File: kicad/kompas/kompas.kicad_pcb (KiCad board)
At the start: 2 copper layers, 59.2 x 130 mm, 81 parts, among them J10 Conn_01x10_Male, J11 Conn_01x10_Male, J12 Conn_01x10_Male, J13 Conn_01x10_Male, J14 Conn_01x10_Male, J15 Conn_01x10_Male, J16 Conn_01x10_Male, J18 Conn_01x10_Male, J19 Conn_01x10_Male, J20 Conn_01x10_Male, J4 Conn_02x05_Odd_Even, J5 Conn_01x06, J6 Conn_01x10_Male, J7 Conn_01x10_Male, J8 Conn_01x10_Male, J9 Conn_01x10_Male, Q1 2N3904, Q2 2N3904, Q3 2N3904, Q4 2N3904, Q5 2N3904, U1 ATmega328-AU, U2 MCP6004, U3 7805_PINS, Y1 Crystal_GND2

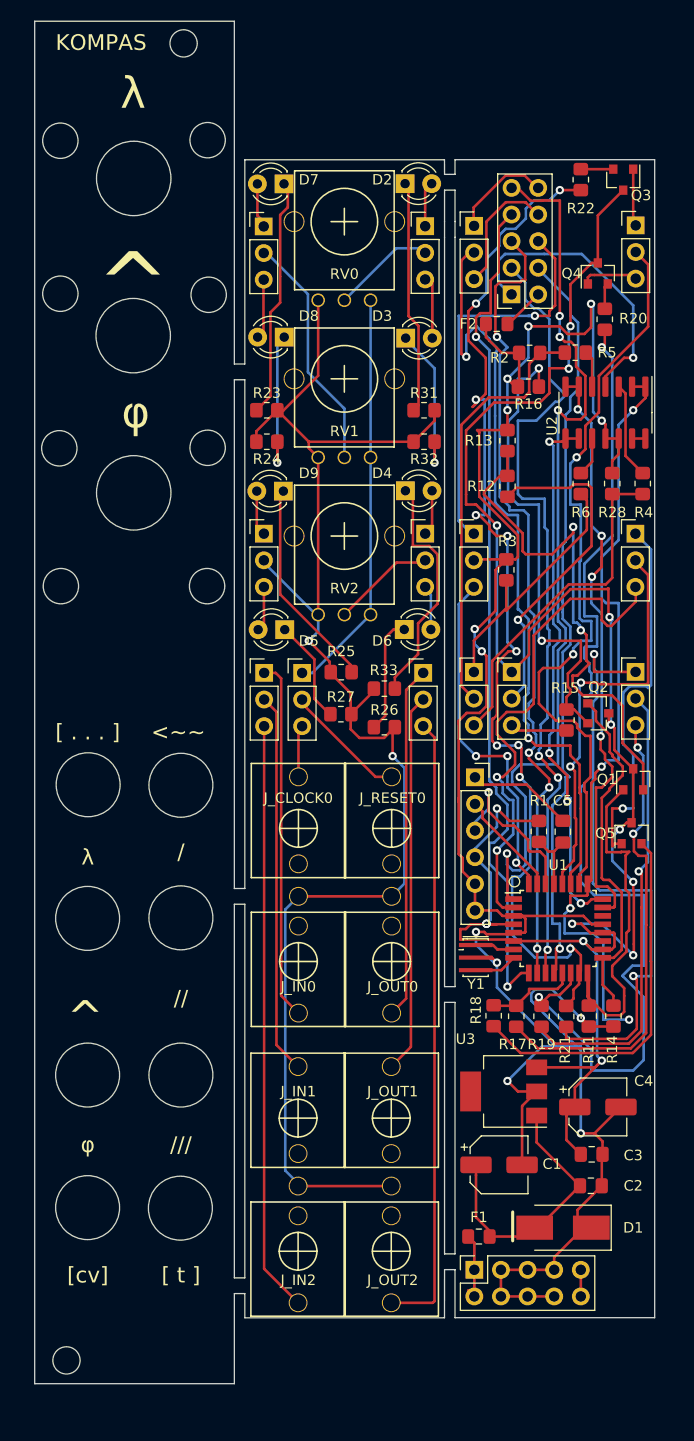
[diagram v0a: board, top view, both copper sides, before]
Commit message: fix transistors
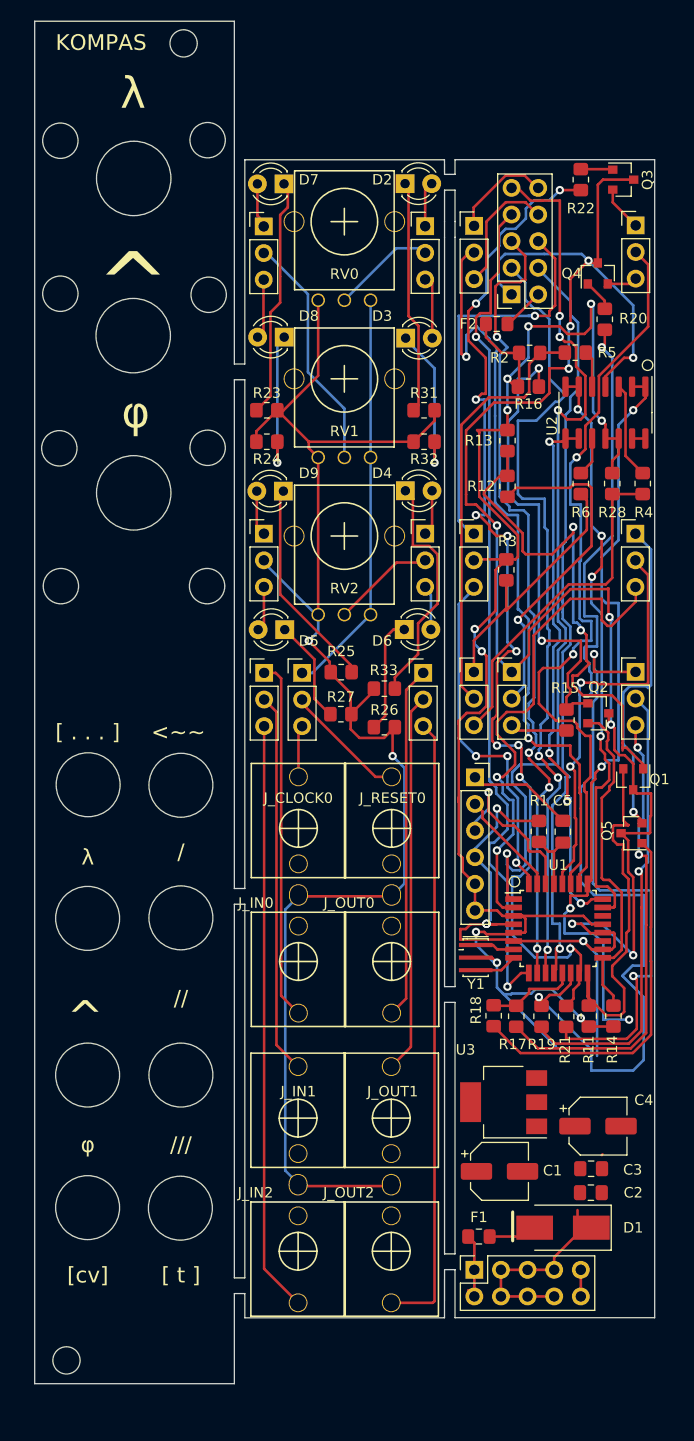
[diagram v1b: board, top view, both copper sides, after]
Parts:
- removed G***: LOGO, custom_eurorack:mates_smaller
- J_IN0, J_IN2, J_OUT0, J_OUT2: value PJ301M-12_without_ground -> PJ301M-12; footprint custom_eurorack:PJ301M-12_without_ground -> eurocad:PJ301M-12
- moved C4 1.83 mm to (122.6, 130.3)
- moved C3 1.37 mm to (121.9, 134.4)
- moved U3 1.02 mm to (113.6, 128.0)
- moved C2 0.66 mm to (121.9, 136.7)
- moved C1 0.63 mm to (113.2, 134.6)
- turned Q1 to 270 degrees
- turned Q3 to 0 degrees
- turned Q5 to 180 degrees
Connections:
- Q1 pad 1: RESET -> Net-(Q1-Pad1)
- Q1 pad 2: Net-(Q1-Pad2) -> RESET
- Q2 pad 1: CLOCK -> Net-(Q2-Pad1)
- Q2 pad 2: Net-(Q2-Pad2) -> CLOCK
- Q3 pad 1: OUT_LED0_B -> Net-(Q3-Pad1)
- Q3 pad 2: Net-(Q3-Pad2) -> OUT_LED0_B
- Q4 pad 1: OUT_LED1_B -> Net-(Q4-Pad1)
- Q4 pad 2: Net-(Q4-Pad2) -> OUT_LED1_B
- Q5 pad 1: OUT_LED2_B -> Net-(Q5-Pad1)
- Q5 pad 2: Net-(Q5-Pad2) -> OUT_LED2_B
- R12 pad 1: Net-(Q1-Pad2) -> Net-(Q1-Pad1)
- R13 pad 1: Net-(Q1-Pad2) -> Net-(Q1-Pad1)
- R15 pad 1: Net-(Q2-Pad2) -> Net-(Q2-Pad1)
- R16 pad 1: Net-(Q2-Pad2) -> Net-(Q2-Pad1)
- R18 pad 1: Net-(Q5-Pad2) -> Net-(Q5-Pad1)
- R20 pad 1: Net-(Q4-Pad2) -> Net-(Q4-Pad1)
- R22 pad 1: Net-(Q3-Pad2) -> Net-(Q3-Pad1)
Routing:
- net Net-(Q1-Pad2): track 50.0 -> 0.00 mm, vias 2 -> 0
- net Net-(Q1-Pad1): track 0.00 -> 48.5 mm, vias 0 -> 2
- net Net-(Q2-Pad2): track 47.0 -> 0.00 mm, vias 2 -> 0
- net Net-(Q2-Pad1): track 0.00 -> 46.7 mm, vias 0 -> 2
- net GND_B: track 222.3 -> 176.1 mm, vias 12 -> 10
- net Net-(Q5-Pad1): track 0.00 -> 35.4 mm
- net Net-(Q5-Pad2): track 35.4 -> 0.00 mm
- net Net-(C1-Pad1): track 26.4 -> 4.68 mm
- net VCC_B: track 222.5 -> 211.2 mm, vias 15 -> 13
- net OUT_LED2_B: track 36.9 -> 32.0 mm
- net Net-(Q3-Pad2): track 3.10 -> 0.00 mm
- net Net-(Q3-Pad1): track 0.00 -> 3.07 mm
- net Net-(Q4-Pad1): track 0.00 -> 3.04 mm
- net Net-(Q4-Pad2): track 2.49 -> 0.00 mm
- net OUT_LED1_B: track 5.30 -> 3.28 mm
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
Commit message: adapt headers
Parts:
- J5: value Conn_01x06 -> Conn_01x07; footprint Connector_PinSocket_2.54mm:PinSocket_1x06_P2.54mm_Vertical -> Connector_PinSocket_2.54mm:PinSocket_1x07_P2.54mm_Vertical
- moved R21 41.2 mm to (100.1, 83.6), turned to 0 degrees
- moved R19 32.6 mm to (98.1, 93.5), turned to 0 degrees
- moved R17 28.3 mm to (102.1, 94.5), turned to 180 degrees
- moved R18 16.6 mm to (127.0, 111.5), turned to 270 degrees
- moved R14 5.20 mm to (118.9, 119.6)
- moved Y1 3.90 mm to (111.3, 118.1), turned to 0 degrees
- moved R33 1.69 mm to (102.2, 86.9)
- moved R26 0.80 mm to (102.2, 91.4)
- moved R11 0.54 mm to (121.4, 119.4)
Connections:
- J10 pad 1: OUT0_B -> OUT0
- J10 pad 2: OUT1_B -> OUT1
- J10 pad 3: OUT2_B -> OUT2
- J4 pad 3: PD7 -> SCK
- J4 pad 4: PB0 -> MISO
- J5 pad 6: GND_B -> SDA
- J_OUT0 pad 3: OUT0_T -> Net-(J_OUT0-Pad3)
- J_OUT1 pad 3: OUT1_T -> Net-(J_OUT1-Pad3)
- J_OUT2 pad 3: OUT2_T -> Net-(J_OUT2-Pad3)
- R17 pad 1: OUT2_B -> Net-(J_OUT2-Pad3)
- R17 pad 2: OUT2 -> OUT2_T
- R19 pad 1: OUT1_B -> Net-(J_OUT1-Pad3)
- R19 pad 2: OUT1 -> OUT1_T
- R21 pad 1: OUT0_B -> Net-(J_OUT0-Pad3)
- R21 pad 2: OUT0 -> OUT0_T
- U1 pad 1: LED0 -> OUT0
- U1 pad 11: PD7 -> CLOCK
- U1 pad 12: PB0 -> RESET
- U1 pad 15: OUT0 -> LED0
- U1 pad 16: RESET -> MISO
- U1 pad 17: CLOCK -> SCK
- U1 pad 19: Net-(U1-Pad19) -> POT1_B
- U1 pad 22: Net-(U1-Pad22) -> POT2_B
- U1 pad 27: POT1_B -> SDA
- U1 pad 28: POT2_B -> SCL
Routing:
- net SCK: track 0.00 -> 96.1 mm, vias 0 -> 4
- net PD7: track 77.3 -> 0.00 mm, vias 3 -> 0
- net MISO: track 0.00 -> 74.6 mm, vias 0 -> 1
- net PB0: track 73.4 -> 0.00 mm, vias 1 -> 0
- net Net-(J_OUT2-Pad3): track 0.00 -> 59.7 mm
- net OUT0_B: track 56.9 -> 0.00 mm, vias 2 -> 0
- net OUT2_T: track 59.5 -> 5.80 mm
- net Net-(J_OUT0-Pad3): track 0.00 -> 45.7 mm, vias 0 -> 1
- net OUT2_B: track 45.0 -> 0.00 mm, vias 2 -> 0
- net OUT1_B: track 43.6 -> 0.00 mm, vias 1 -> 0
- net Net-(J_OUT1-Pad3): track 0.00 -> 37.1 mm
- net OUT1: track 94.0 -> 129.2 mm, vias 2 -> 6
- net OUT2: track 8.71 -> 42.0 mm, vias 0 -> 2
- net GND_B: track 176.1 -> 206.9 mm, vias 10 -> 8
- net OUT1_T: track 36.3 -> 8.46 mm, vias 0 -> 1
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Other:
- outline, holes or cut-outs redrawn

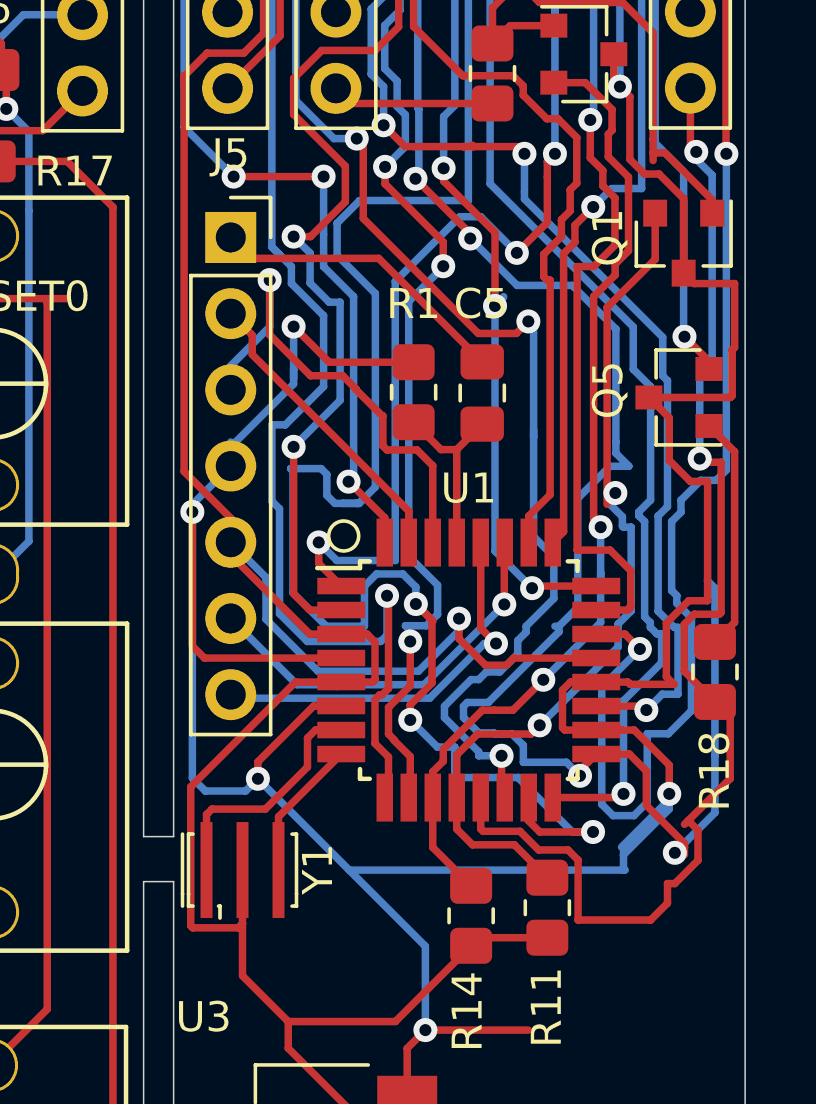
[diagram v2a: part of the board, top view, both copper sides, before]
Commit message: add SS header
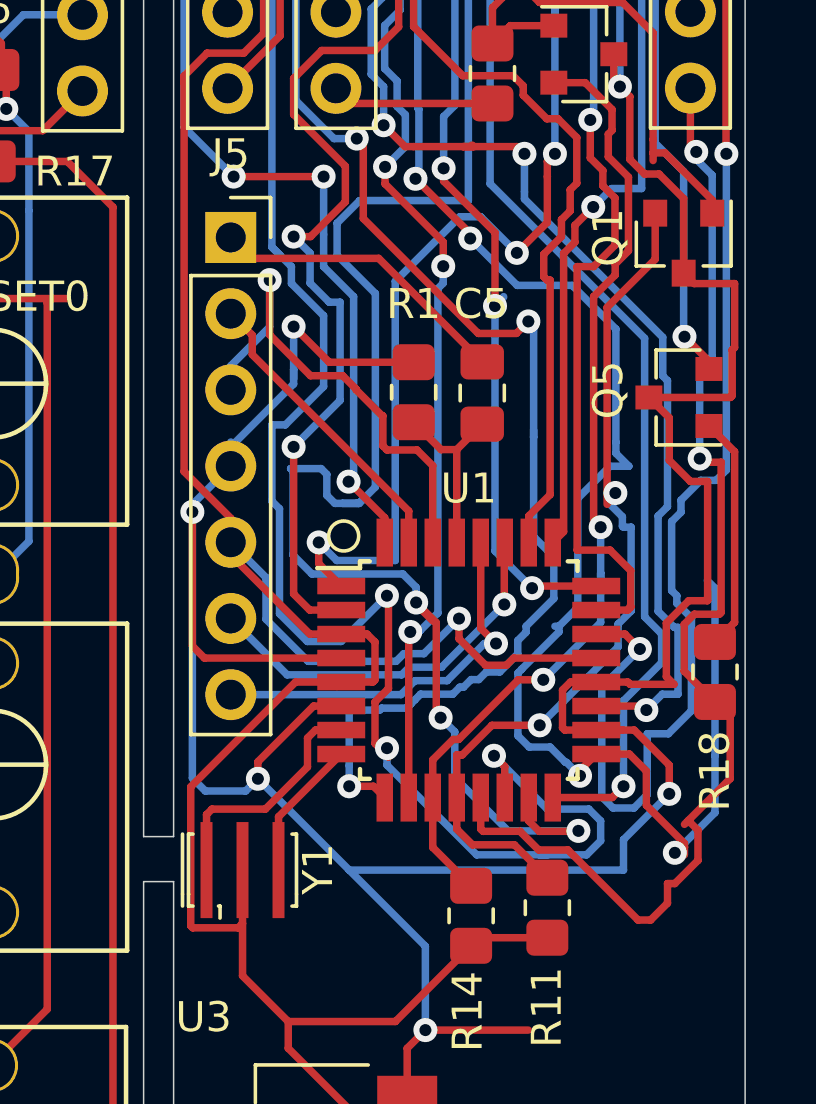
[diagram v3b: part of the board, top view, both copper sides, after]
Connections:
- U1 pad 14: OUT1 -> LED1
- U1 pad 9: LED1 -> OUT1
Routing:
- net LED1: track 84.5 -> 98.9 mm, vias 2 -> 4
- net LED0: track 111.8 -> 107.2 mm
- net OUT1: track 129.2 -> 132.2 mm
- net SCK: track 96.1 -> 93.2 mm
- net VCC_B: track 236.4 -> 233.8 mm
- net LED2: track 78.5 -> 77.1 mm
- net OUT2: track 42.0 -> 40.8 mm
- net MISO: track 74.6 -> 74.0 mm
- net POT2_B: track 51.4 -> 50.9 mm
- net GND_B: track 206.9 -> 206.4 mm
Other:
- board text added: "MISO|PB4"
- board text added: "MOSI|LED0"
- board text added: "SCK|PB5"
- board text added: "SCL"
- board text added: "SDA"
- board text added: "SS|LED1"
- board text removed: "LED0"
- board text removed: "LED1"
- board text removed: "PB0"
- board text removed: "PD7"

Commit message: fixup reset pin
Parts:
- removed C5: 100n, Capacitor_SMD:C_0805_2012Metric_Pad1.18x1.45mm_HandSolder
- J_IN0, J_IN2, J_OUT0, J_OUT2: value PJ301M-12 -> PJ301M-12-2hole; footprint eurocad:PJ301M-12 -> graphics:PJ301M-12-2hole
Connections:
- J5 pad 1: Net-(C5-Pad1) -> RST
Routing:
- net RST: track 6.11 -> 17.8 mm
- net Net-(C5-Pad1): track 10.1 -> 0.00 mm
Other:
- board text added: "KOMPAS STZIOPA // BASTL ___________________ | smd by PHILOMATES | | bottom__rev 2 |"
- board text added: "|smd by PHILOMATES| top__rev2"
- board text removed: "JLCJLCJLCJLC"
- board text removed: "KOMPAS STZIOPA // BASTL ___________________ | smd by PHILOMATES | | bottom__rev 1 |"
- board text removed: "|smd by PHILOMATES| top__rev1"

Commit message: rev3
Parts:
- removed F2: Polyfuse, Fuse:Fuse_0805_2012Metric_Pad1.15x1.40mm_HandSolder
- added G***: LOGO, graphics:mates, B.Cu at (118.6, 121.2)
- J4: footprint Connector_PinSocket_2.54mm:PinSocket_2x05_P2.54mm_Vertical -> Connector_PinSocket_2.54mm:PinSocket_2x04_P2.54mm_Vertical
- R17, R19, R21, R23, R24, R25, R26, R27, R31, R32, R33: moved to B.Cu
- moved R25 23.9 mm to (91.4, 64.0), turned to 270 degrees
- moved R23 22.8 mm to (98.4, 40.4)
- moved R31 16.9 mm to (98.4, 47.0), turned to 180 degrees
- moved R17 14.8 mm to (98.0, 108.7), turned to 90 degrees
- moved R33 14.7 mm to (98.3, 72.6)
- moved R24 12.1 mm to (98.1, 55.1)
- moved R19 10.3 mm to (90.4, 100.3), turned to 90 degrees
- moved R27 9.57 mm to (98.3, 100.6), turned to 90 degrees
- moved R26 9.03 mm to (106.2, 99.6), turned to 270 degrees
- moved R32 8.90 mm to (98.1, 61.0)
- moved R21 3.74 mm to (98.3, 80.3)
- moved RV2 2.88 mm to (98.4, 76.9)
- moved J4 2.48 mm to (114.4, 48.5)
- moved D6 1.19 mm to (105.0, 83.7), turned to 45 degrees
- moved D5 0.98 mm to (92.1, 83.7), turned to 135 degrees
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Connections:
- J4 pad 1: VCC_B -> SCK
- J4 pad 2: Net-(F2-Pad2) -> MISO
- J4 pad 3: SCK -> LED2
- J4 pad 4: MISO -> LED2_A_B
- J4 pad 5: LED2 -> LED1
- J4 pad 6: LED2_A_B -> LED1_A_B
- J4 pad 7: LED1 -> LED0
- J4 pad 8: LED1_A_B -> LED0_A_B
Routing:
- net Net-(D4-Pad1): track 28.2 -> 6.14 mm
- net Net-(J_OUT2-Pad3): track 59.7 -> 39.4 mm
- net Net-(D7-Pad1): track 23.0 -> 4.81 mm
- net Net-(D5-Pad1): track 9.84 -> 24.7 mm, vias 0 -> 2
- net OUT2_T: track 5.80 -> 20.5 mm
- net GND_T: track 143.4 -> 158.1 mm, vias 2 -> 0
- net Net-(D2-Pad1): track 22.3 -> 9.24 mm
- net VCC_B: track 233.8 -> 220.9 mm
- net Net-(D9-Pad1): track 20.2 -> 8.03 mm
- net OUT1_T: track 8.46 -> 19.5 mm, vias 1 -> 0
- net VCC_T: track 39.5 -> 47.4 mm
- net Net-(J_OUT0-Pad3): track 45.7 -> 53.0 mm, vias 1 -> 0
- net Net-(D3-Pad1): track 15.2 -> 8.01 mm, vias 1 -> 0
- net Net-(D8-Pad1): track 14.3 -> 7.32 mm, vias 1 -> 0
- net Net-(J_OUT1-Pad3): track 37.1 -> 30.2 mm
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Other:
- board size 59.2 x 130 mm -> 59.2 x 128.6 mm
- board text added: "KOMPAS STZIOPA // BASTL ___________________ | smd by PHILOMATES | | bottom__rev 3 |"
- board text added: "|smd by PHILOMATES| top__rev3"
- board text removed: "KOMPAS STZIOPA // BASTL ___________________ | smd by PHILOMATES | | bottom__rev 2 |"
- board text removed: "|smd by PHILOMATES| top__rev2"

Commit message: add some libs
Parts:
- removed G***: LOGO, graphics:mates
- J_IN0, J_IN2, J_OUT0, J_OUT2: value PJ301M-12-2hole -> PJ301M-12; footprint graphics:PJ301M-12-2hole -> eurocad:PJ301M-12-2hole
